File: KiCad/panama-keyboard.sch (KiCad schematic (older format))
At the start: 170 parts, among them J1 MX, J2 USB_C_Receptacle_USB2.0, J3 AVR-ISP-6, K1 MX, M1 MX, P1 MX, Q1 MX, T1 MX, U1 MX, U2 ATmega32A-PU, X1 MX, Y1 MX, Y2 Crystal

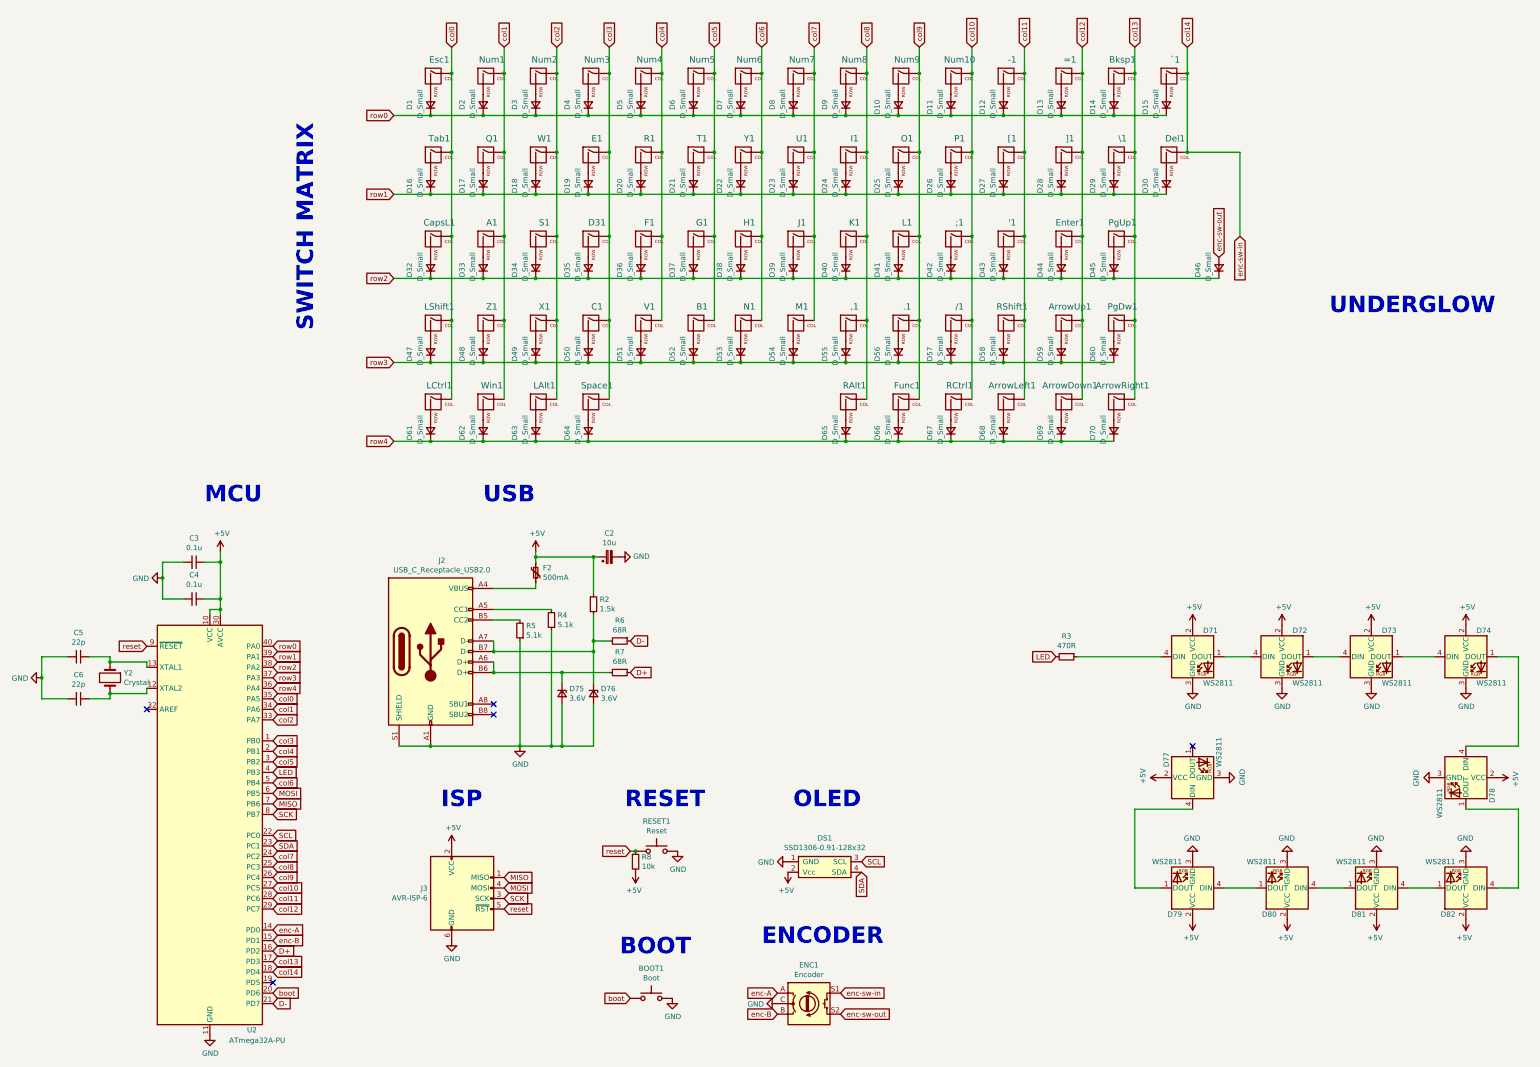
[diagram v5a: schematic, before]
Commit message: pinout changed, pcb trace to be reworked
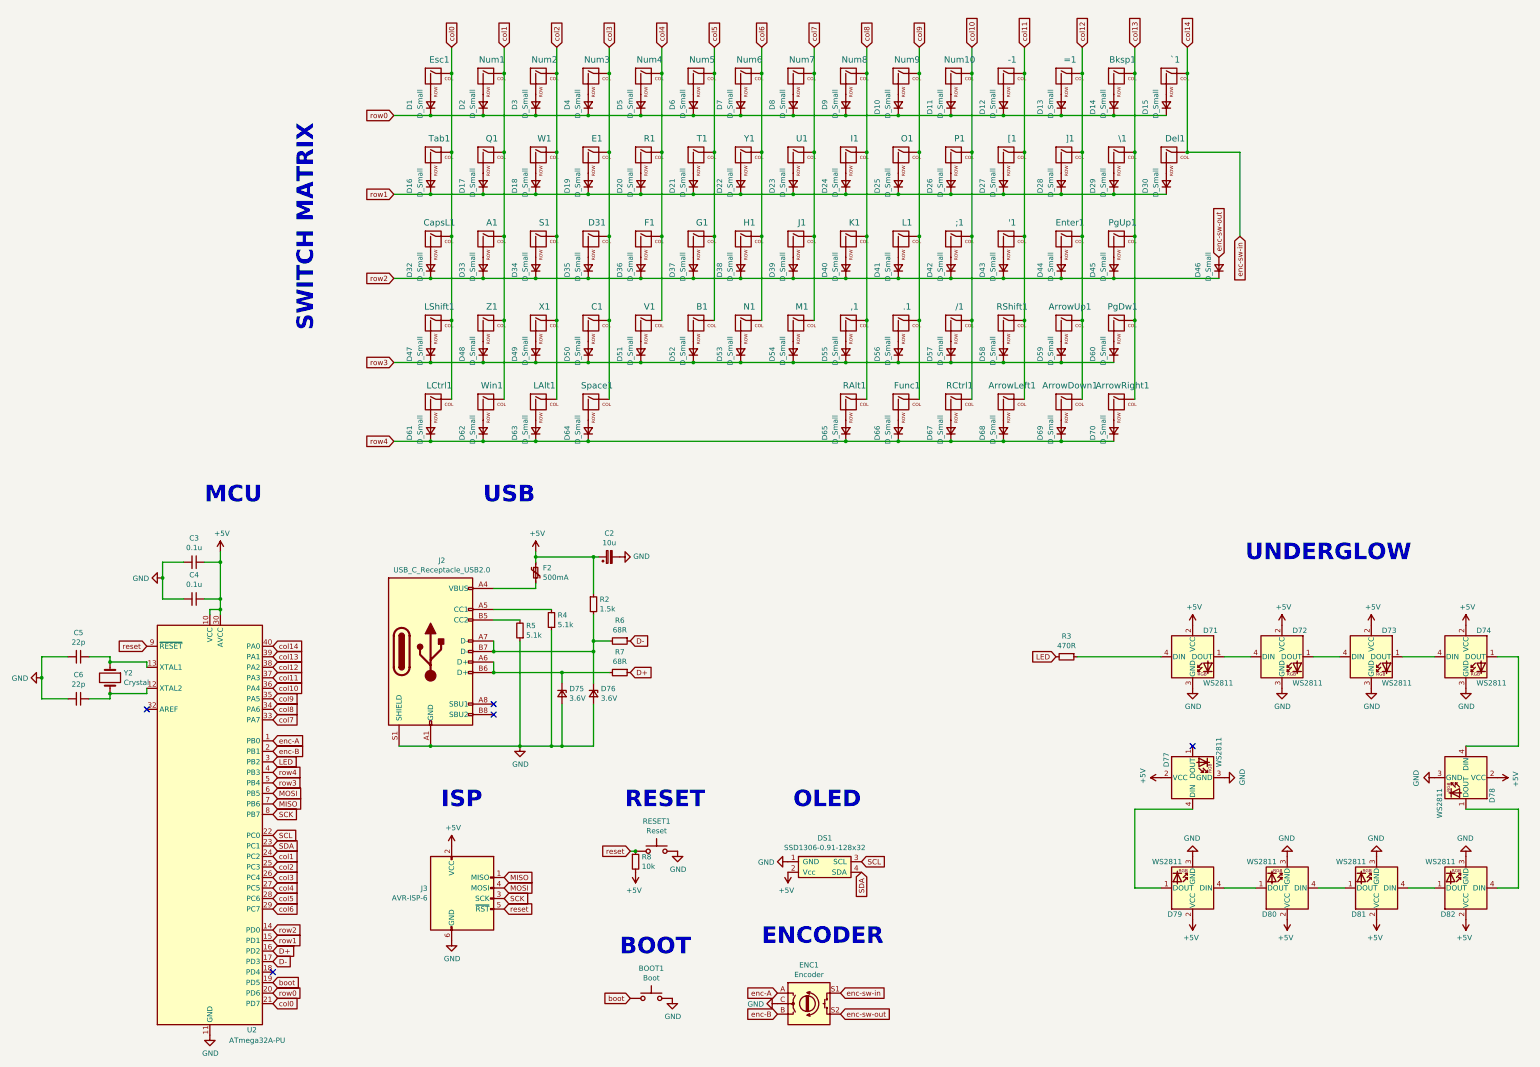
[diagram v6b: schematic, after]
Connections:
- net D-: now also U2.17 (PD3); no longer U2.21 (PD7)
- net LED: now also U2.3 (PB2); no longer U2.4 (PB3)
- net boot: now also U2.19 (PD5); no longer U2.20 (PD6)
- net col0: now also U2.21 (PD7); no longer U2.35 (PA5)
- net col1: now also U2.24 (PC2); no longer U2.34 (PA6)
- net col10: now also U2.36 (PA4); no longer U2.27 (PC5)
- net col11: now also U2.37 (PA3); no longer U2.28 (PC6)
- net col12: now also U2.38 (PA2); no longer U2.29 (PC7)
- net col13: now also U2.39 (PA1); no longer U2.17 (PD3)
- net col14: now also U2.40 (PA0); no longer U2.18 (PD4)
- net col2: now also U2.25 (PC3); no longer U2.33 (PA7)
- net col3: now also U2.26 (PC4); no longer U2.1 (PB0)
- net col4: now also U2.27 (PC5); no longer U2.2 (PB1)
- net col5: now also U2.28 (PC6); no longer U2.3 (PB2)
- net col6: now also U2.29 (PC7); no longer U2.5 (PB4)
- net col7: now also U2.33 (PA7); no longer U2.24 (PC2)
- net col8: now also U2.34 (PA6); no longer U2.25 (PC3)
- net col9: now also U2.35 (PA5); no longer U2.26 (PC4)
- net enc-A: now also U2.1 (PB0); no longer U2.14 (PD0)
- net enc-B: now also U2.2 (PB1); no longer U2.15 (PD1)
- net row0: now also U2.20 (PD6); no longer U2.40 (PA0)
- net row1: now also U2.15 (PD1); no longer U2.39 (PA1)
- net row2: now also U2.14 (PD0); no longer U2.38 (PA2)
- net row3: now also U2.5 (PB4); no longer U2.37 (PA3)
- net row4: now also U2.4 (PB3); no longer U2.36 (PA4)
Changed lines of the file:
@@
 Text GLabel 4450 4950 0    50   Input ~ 0
 row4
-$Comp
-L MCU_Microchip_ATmega:ATmega32A-PU U2
-U 1 1 5F24C56F
-P 2700 8600
-F 0 "U2" H 3100 6650 50  0000 C CNN
-F 1 "ATmega32A-PU" H 3150 6550 50  0000 C CNN
-F 2 "Package_DIP:DIP-40_W15.24mm_Socket" H 2700 8600 50  0001 C CIN
-F 3 "http://ww1.microchip.com/downloads/en/DeviceDoc/atmel-8155-8-bit-microcontroller-avr-atmega32a_datasheet.pdf" H 2700 8600 50  0001 C CNN
-	1    2700 8600
-	1    0    0    -1
-$EndComp
 Text Notes 3700 3900 1    157  ~ 31
 SWITCH MATRIX
-Text Notes 13350 3750 0    157  ~ 31
+Text Notes 12550 6100 0    157  ~ 31
 UNDERGLOW
 Text Notes 6600 9850 0    157  ~ 31
@@
 Text Notes 2650 5550 0    157  ~ 31
 MCU
-Text GLabel 3300 8400 2    50   Input ~ 0
-MISO
-Text GLabel 3300 8300 2    50   Input ~ 0
-MOSI
-Text GLabel 3300 8500 2    50   Input ~ 0
-SCK
-Text GLabel 3300 10200 2    50   Input ~ 0
+Text GLabel 3300 10100 2    50   Input ~ 0
 boot
 Text GLabel 3300 8700 2    50   Input ~ 0
@@
 Text GLabel 3300 8800 2    50   Input ~ 0
 SDA
-Text GLabel 3300 8100 2    50   Input ~ 0
-LED
-Text GLabel 3300 9700 2    50   Input ~ 0
-enc-B
-Text GLabel 3300 10300 2    50   Input ~ 0
+Text GLabel 3300 9900 2    50   Input ~ 0
 D-
 Text GLabel 3300 9800 2    50   Input ~ 0
@@
 	0    1    1    0
 $EndComp
+Text GLabel 3300 10200 2    50   Input ~ 0
+row0
+Text GLabel 3300 9700 2    50   Input ~ 0
+row1
+Text GLabel 3300 9600 2    50   Input ~ 0
+row2
+Text GLabel 3300 8200 2    50   Input ~ 0
+row3
+Text GLabel 3300 8100 2    50   Input ~ 0
+row4
+Text GLabel 3300 10300 2    50   Input ~ 0
+col0
+Text GLabel 3300 8900 2    50   Input ~ 0
+col1
+Text GLabel 3300 9000 2    50   Input ~ 0
+col2
+Text GLabel 3300 9100 2    50   Input ~ 0
+col3
+Text GLabel 3300 7600 2    50   Input ~ 0
+col7
+Text GLabel 3300 7500 2    50   Input ~ 0
+col8
+Text GLabel 3300 7400 2    50   Input ~ 0
+col9
+Text GLabel 3300 7300 2    50   Input ~ 0
+col10
+Text GLabel 3300 7200 2    50   Input ~ 0
+col11
+Text GLabel 3300 7100 2    50   Input ~ 0
+col12
+Text GLabel 3300 7000 2    50   Input ~ 0
+col13
 Text GLabel 3300 6900 2    50   Input ~ 0
-row0
-Text GLabel 3300 7000 2    50   Input ~ 0
-row1
-Text GLabel 3300 7100 2    50   Input ~ 0
-row2
-Text GLabel 3300 7200 2    50   Input ~ 0
-row3
-Text GLabel 3300 7300 2    50   Input ~ 0
-row4
-Text GLabel 3300 7400 2    50   Input ~ 0
-col0
-Text GLabel 3300 7500 2    50   Input ~ 0
-col1
-Text GLabel 3300 7600 2    50   Input ~ 0
-col2
+col14
 Text GLabel 3300 7800 2    50   Input ~ 0
-col3
-Text GLabel 3300 7900 2    50   Input ~ 0
-col4
-Text GLabel 3300 8000 2    50   Input ~ 0
-col5
-Text GLabel 3300 8200 2    50   Input ~ 0
-col6
-Text GLabel 3300 8900 2    50   Input ~ 0
-col7
-Text GLabel 3300 9000 2    50   Input ~ 0
-col8
-Text GLabel 3300 9100 2    50   Input ~ 0
-col9
-Text GLabel 3300 9200 2    50   Input ~ 0
-col10
-Text GLabel 3300 9300 2    50   Input ~ 0
-col11
-Text GLabel 3300 9400 2    50   Input ~ 0
-col12
-Text GLabel 3300 9900 2    50   Input ~ 0
-col13
-Text GLabel 3300 10000 2    50   Input ~ 0
-col14
-Text GLabel 3300 9600 2    50   Input ~ 0
 enc-A
-NoConn ~ 3300 10100
 $Comp
 L Keyboard:MX Y1
@@
 	6300 1850 6800 1850
 Connection ~ 6300 1850
+Text GLabel 3300 9400 2    50   Input ~ 0
+col6
+Text GLabel 3300 9300 2    50   Input ~ 0
+col5
+Text GLabel 3300 9200 2    50   Input ~ 0
+col4
+Text GLabel 3300 7900 2    50   Input ~ 0
+enc-B
+Text GLabel 3300 8000 2    50   Input ~ 0
+LED
+Text GLabel 3300 8500 2    50   Input ~ 0
+SCK
+Text GLabel 3300 8300 2    50   Input ~ 0
+MOSI
+Text GLabel 3300 8400 2    50   Input ~ 0
+MISO
+$Comp
+L MCU_Microchip_ATmega:ATmega32A-PU U2
+U 1 1 5F24C56F
+P 2700 8600
+F 0 "U2" H 3100 6650 50  0000 C CNN
+F 1 "ATmega32A-PU" H 3150 6550 50  0000 C CNN
+F 2 "Package_DIP:DIP-40_W15.24mm_Socket" H 2700 8600 50  0001 C CIN
+F 3 "http://ww1.microchip.com/downloads/en/DeviceDoc/atmel-8155-8-bit-microcontroller-avr-atmega32a_datasheet.pdf" H 2700 8600 50  0001 C CNN
+	1    2700 8600
+	1    0    0    -1
+$EndComp
+NoConn ~ 3300 10000
 $EndSCHEMATC

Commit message: traces removed for new pinout
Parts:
- BOOT1, RESET1: symbol Switch:SW_Push -> panama-keyboard-rescue:SW_Push-Switch
- C2: symbol Device:CP_Small -> panama-keyboard-rescue:CP_Small-Device
- C3, C4, C5, C6: symbol Device:C_Small -> panama-keyboard-rescue:C_Small-Device
- D1, D10, D11, D12, D13, D14, D15, D16, D17, D18, D19, D2, D20, D21, D22, D23, D24, D25, D26, D27, D28, D29, D3, D30, D32, D33, D34, D35, D36, D37, D38, D39, D4, D40, D41, D42, D43, D44, D45, D46, D47, D48, D49, D5, D50, D51, D52, D53, D54, D55, D56, D57, D58, D59, D6, D60, D61, D62, D63, D64, D65, D66, D67, D68, D69, D7, D70, D8, D9: symbol Device:D_Small -> panama-keyboard-rescue:D_Small-Device
- D75, D76: symbol Device:D_Zener_Small -> panama-keyboard-rescue:D_Zener_Small-Device
- ENC1: symbol Device:Rotary_Encoder_Switch -> panama-keyboard-rescue:Rotary_Encoder_Switch-Device
- F2: symbol Device:Polyfuse_Small -> panama-keyboard-rescue:Polyfuse_Small-Device
- J2: symbol Connector:USB_C_Receptacle_USB2.0 -> panama-keyboard-rescue:USB_C_Receptacle_USB2.0-Connector
- J3: symbol Connector:AVR-ISP-6 -> panama-keyboard-rescue:AVR-ISP-6-Connector
- R2, R3, R4, R5, R6, R7, R8: symbol Device:R_Small -> panama-keyboard-rescue:R_Small-Device
- U2: symbol MCU_Microchip_ATmega:ATmega32A-PU -> panama-keyboard-rescue:ATmega32A-PU-MCU_Microchip_ATmega
- Y2: symbol Device:Crystal -> panama-keyboard-rescue:Crystal-Device
